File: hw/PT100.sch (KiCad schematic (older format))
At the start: 2 parts, among them U1501 ZXCT1086

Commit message: pcb first revision created, ready to order
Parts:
- removed U1501: ZXCT1086, usevolt:SOT-25, symbol ZXCT1086
- added U1601: ZXCT1086, usevolt:SOT-25, symbol ZXCT1086
- renumbered R1501 to R1401
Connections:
- net +3V3: now also U1601.5 (VCC)
- net GND: now also U1601.2 (GND), U1601.4 (S-)
- net VOUT: now also U1601.1 (OUT)
- net SENSE+ renamed SENSOR
- net SENSOR: now also U1601.3 (S+)
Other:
- moved on the sheet: R1701
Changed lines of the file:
@@
 EESchema Schematic File Version 2
-LIBS:msb-rescue
 LIBS:kemet
 LIBS:multicomp
@@
 LIBS:power
 LIBS:elt21300_kicad
-LIBS:msb-cache
+LIBS:esb-cache
 EELAYER 26 0
 EELAYER END
 $Descr A4 11693 8268
 encoding utf-8
-Sheet 15 16
+Sheet 16 17
 Title ""
 Date ""
@@
 Comment4 ""
 $EndDescr
-Text HLabel 6300 3250 0    60   Input ~ 0
-SENSE+
-Text HLabel 6300 4100 0    60   Input ~ 0
-SENSE-
-Text HLabel 7650 3700 2    60   Output ~ 0
+Text HLabel 7800 3600 2    60   Input ~ 0
+SENSOR
+Text HLabel 6450 3700 0    60   Output ~ 0
 VOUT
+Wire Wire Line
+	7450 3600 7800 3600
+Wire Wire Line
+	7600 3600 7600 3250
 $Comp
-L 10K R1501
-U 1 1 58C98806
-P 6500 3050
-AR Path="/58C97F3A/58C98806" Ref="R1501"  Part="1"
-AR Path="/58CA60CA/58C98806" Ref="R1601"  Part="1"
-F 0 "R1601" V 6508 3108 45  0000 L CNN
-F 1 "10K" V 6592 3108 45  0000 L CNN
-F 2 "multicomp:0603" H 6530 3200 20  0001 C CNN
-F 3 "http://www.farnell.com/datasheets/1788326.pdf?_ga=1.214208087.1948984246.1460023966" H 6469 3089 60  0001 C CNN
-F 4 "9330399" H 6869 3489 60  0001 C CNN "1st Source Part Number"
-F 5 "Farnell" H 6769 3389 60  0001 C CNN "1st Source"
-F 6 "MC0063W0603110K" H 6669 3289 60  0001 C CNN "Manufacturer Part Number"
-F 7 "MULTICOMP" H 6569 3189 60  0001 C CNN "Manufacturer"
-	1    6500 3050
-	0    1    1    0
+L GND #PWR1402
+U 1 1 58C99E8C
+P 6750 4000
+AR Path="/58C97F3A/58C99E8C" Ref="#PWR1402"  Part="1"
+AR Path="/58CA60CA/58C99E8C" Ref="#PWR1502"  Part="1"
+AR Path="/594BBBEF/58C99E8C" Ref="#PWR1602"  Part="1"
+AR Path="/594D630A/58C99E8C" Ref="#PWR1702"  Part="1"
+F 0 "#PWR1702" H 6750 3750 50  0001 C CNN
+F 1 "GND" H 6755 3827 50  0000 C CNN
+F 2 "" H 6750 4000 50  0000 C CNN
+F 3 "" H 6750 4000 50  0000 C CNN
+	1    6750 4000
+	-1   0    0    -1
+$EndComp
+Wire Wire Line
+	6750 4000 6750 3800
+Wire Wire Line
+	6750 3800 6900 3800
+$Comp
+L +3V3 #PWR1401
+U 1 1 58C99EAF
+P 6750 3400
+AR Path="/58C97F3A/58C99EAF" Ref="#PWR1401"  Part="1"
+AR Path="/58CA60CA/58C99EAF" Ref="#PWR1501"  Part="1"
+AR Path="/594BBBEF/58C99EAF" Ref="#PWR1601"  Part="1"
+AR Path="/594D630A/58C99EAF" Ref="#PWR1701"  Part="1"
+F 0 "#PWR1701" H 6750 3250 50  0001 C CNN
+F 1 "+3V3" H 6765 3573 50  0000 C CNN
+F 2 "" H 6750 3400 50  0000 C CNN
+F 3 "" H 6750 3400 50  0000 C CNN
+	1    6750 3400
+	-1   0    0    -1
+$EndComp
+Wire Wire Line
+	6750 3400 6750 3600
+Wire Wire Line
+	6750 3600 6900 3600
+Wire Wire Line
+	6450 3700 6900 3700
+Wire Wire Line
+	7600 2850 7600 2950
+$Comp
+L +3V3 #PWR1403
+U 1 1 58C98CB1
+P 7600 2850
+AR Path="/58C97F3A/58C98CB1" Ref="#PWR1403"  Part="1"
+AR Path="/58CA60CA/58C98CB1" Ref="#PWR1503"  Part="1"
+AR Path="/594BBBEF/58C98CB1" Ref="#PWR1603"  Part="1"
+AR Path="/594D630A/58C98CB1" Ref="#PWR1703"  Part="1"
+F 0 "#PWR1703" H 7600 2700 50  0001 C CNN
+F 1 "+3V3" H 7615 3023 50  0000 C CNN
+F 2 "" H 7600 2850 50  0000 C CNN
+F 3 "" H 7600 2850 50  0000 C CNN
+	1    7600 2850
+	-1   0    0    -1
 $EndComp
 $Comp
-L +3V3 #PWR1501
-U 1 1 58C98CB1
-P 6500 2850
-AR Path="/58C97F3A/58C98CB1" Ref="#PWR1501"  Part="1"
-AR Path="/58CA60CA/58C98CB1" Ref="#PWR1601"  Part="1"
-F 0 "#PWR1601" H 6500 2700 50  0001 C CNN
-F 1 "+3V3" H 6515 3023 50  0000 C CNN
-F 2 "" H 6500 2850 50  0000 C CNN
-F 3 "" H 6500 2850 50  0000 C CNN
-	1    6500 2850
+L 10K R1401
+U 1 1 58C98806
+P 7600 3050
+AR Path="/58C97F3A/58C98806" Ref="R1401"  Part="1"
+AR Path="/58CA60CA/58C98806" Ref="R1501"  Part="1"
+AR Path="/594BBBEF/58C98806" Ref="R1601"  Part="1"
+AR Path="/594D630A/58C98806" Ref="R1701"  Part="1"
+F 0 "R1701" V 7608 3108 45  0000 L CNN
+F 1 "10K" V 7692 3108 45  0000 L CNN
+F 2 "multicomp:0603" H 7630 3200 20  0001 C CNN
+F 3 "http://www.farnell.com/datasheets/1788326.pdf?_ga=1.214208087.1948984246.1460023966" H 7569 3089 60  0001 C CNN
+F 4 "9330399" H 7969 3489 60  0001 C CNN "1st Source Part Number"
+F 5 "Farnell" H 7869 3389 60  0001 C CNN "1st Source"
+F 6 "MC0063W0603110K" H 7769 3289 60  0001 C CNN "Manufacturer Part Number"
+F 7 "MULTICOMP" H 7669 3189 60  0001 C CNN "Manufacturer"
+	1    7600 3050
+	0    -1   1    0
+$EndComp
+Connection ~ 7600 3600
+$Comp
+L GND #PWR1404
+U 1 1 5944CE5C
+P 7600 3900
+AR Path="/58C97F3A/5944CE5C" Ref="#PWR1404"  Part="1"
+AR Path="/58CA60CA/5944CE5C" Ref="#PWR1504"  Part="1"
+AR Path="/594BBBEF/5944CE5C" Ref="#PWR1604"  Part="1"
+AR Path="/594D630A/5944CE5C" Ref="#PWR1704"  Part="1"
+F 0 "#PWR1704" H 7600 3650 50  0001 C CNN
+F 1 "GND" H 7605 3727 50  0000 C CNN
+F 2 "" H 7600 3900 50  0000 C CNN
+F 3 "" H 7600 3900 50  0000 C CNN
+	1    7600 3900
 	1    0    0    -1
 $EndComp
 Wire Wire Line
-	6500 2850 6500 2950
+	7600 3900 7600 3800
 Wire Wire Line
-	6500 3250 6300 3250
+	7600 3800 7450 3800
 $Comp
-L ZXCT1086 U1501
-U 1 1 58C999D0
-P 6900 3650
-AR Path="/58C97F3A/58C999D0" Ref="U1501"  Part="1"
-AR Path="/58CA60CA/58C999D0" Ref="U1601"  Part="1"
-F 0 "U1601" H 6875 3937 60  0000 C CNN
-F 1 "ZXCT1086" H 6875 3831 60  0000 C CNN
-F 2 "usevolt:SOT-25" H 6550 4100 60  0001 C CNN
-F 3 "http://www.farnell.com/datasheets/1383709.pdf?_ga=1.188141032.1948984246.1460023966" H 7300 3975 60  0001 C CNN
-F 4 "1904029" H 7300 4200 60  0001 C CNN "1st Source Part Number"
-F 5 "Digikey" H 7400 4300 60  0001 C CNN "2nd Source"
-F 6 "DIODES INC" H 7000 3900 60  0001 C CNN "Manufacturer"
-F 7 "Farnell" H 7200 4100 60  0001 C CNN "1st Source"
-F 8 "ZXCT1086E5TA" H 7100 4000 60  0001 C CNN "Manufacturer Part Number"
-F 9 "ZXCT1086E5TACT-ND" H 7500 4400 60  0001 C CNN "2nd Source Part Number"
-	1    6900 3650
-	-1   0    0    -1
-$EndComp
-Wire Wire Line
-	6650 3600 6500 3600
-Wire Wire Line
-	6500 3600 6500 3250
-Wire Wire Line
-	6650 3800 6500 3800
-Wire Wire Line
-	6500 3800 6500 4100
-Wire Wire Line
-	6500 4100 6300 4100
-$Comp
-L GND #PWR1503
-U 1 1 58C99E8C
-P 7350 4000
-AR Path="/58C97F3A/58C99E8C" Ref="#PWR1503"  Part="1"
-AR Path="/58CA60CA/58C99E8C" Ref="#PWR1603"  Part="1"
-F 0 "#PWR1603" H 7350 3750 50  0001 C CNN
-F 1 "GND" H 7355 3827 50  0000 C CNN
-F 2 "" H 7350 4000 50  0000 C CNN
-F 3 "" H 7350 4000 50  0000 C CNN
-	1    7350 4000
+L ZXCT1086 U1601
+U 1 1 5953DA3A
+P 7200 3650
+AR Path="/594BBBEF/5953DA3A" Ref="U1601"  Part="1"
+AR Path="/58C97F3A/5953DA3A" Ref="U1401"  Part="1"
+AR Path="/58CA60CA/5953DA3A" Ref="U1501"  Part="1"
+AR Path="/594D630A/5953DA3A" Ref="U1701"  Part="1"
+F 0 "U1701" H 7175 3937 60  0000 C CNN
+F 1 "ZXCT1086" H 7175 3831 60  0000 C CNN
+F 2 "usevolt:SOT-25" H 6850 4100 60  0001 C CNN
+F 3 "http://www.farnell.com/datasheets/1383709.pdf?_ga=1.188141032.1948984246.1460023966" H 7600 3975 60  0001 C CNN
+F 4 "1904029" H 7600 4200 60  0001 C CNN "1st Source Part Number"
+F 5 "Digikey" H 7700 4300 60  0001 C CNN "2nd Source"
+F 6 "DIODES INC" H 7300 3900 60  0001 C CNN "Manufacturer"
+F 7 "Farnell" H 7500 4100 60  0001 C CNN "1st Source"
+F 8 "ZXCT1086E5TA" H 7400 4000 60  0001 C CNN "Manufacturer Part Number"
+F 9 "ZXCT1086E5TACT-ND" H 7800 4400 60  0001 C CNN "2nd Source Part Number"
+	1    7200 3650
 	1    0    0    -1
 $EndComp
-Wire Wire Line
-	7350 4000 7350 3800
-Wire Wire Line
-	7350 3800 7200 3800
-$Comp
-L +3V3 #PWR1502
-U 1 1 58C99EAF
-P 7350 3400
-AR Path="/58C97F3A/58C99EAF" Ref="#PWR1502"  Part="1"
-AR Path="/58CA60CA/58C99EAF" Ref="#PWR1602"  Part="1"
-F 0 "#PWR1602" H 7350 3250 50  0001 C CNN
-F 1 "+3V3" H 7365 3573 50  0000 C CNN
-F 2 "" H 7350 3400 50  0000 C CNN
-F 3 "" H 7350 3400 50  0000 C CNN
-	1    7350 3400
-	1    0    0    -1
-$EndComp
-Wire Wire Line
-	7350 3400 7350 3600
-Wire Wire Line
-	7350 3600 7200 3600
-Wire Wire Line
-	7650 3700 7200 3700
 $EndSCHEMATC

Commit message: hw modifications from first version
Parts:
- removed U1601: ZXCT1086, usevolt:SOT-25, symbol ZXCT1086
- added U1401: ZXCT1086, usevolt:SOT-25, symbol ZXCT1086
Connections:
- net +3V3: now also U1401.5 (VCC)
- net GND: now also U1401.2 (GND), U1401.4 (S-)
- net SENSOR: now also U1401.3 (S+)
- net VOUT: now also U1401.1 (OUT)
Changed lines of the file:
@@
 $Descr A4 11693 8268
 encoding utf-8
-Sheet 16 17
+Sheet 14 17
 Title ""
 Date ""
@@
 	7600 3800 7450 3800
 $Comp
-L ZXCT1086 U1601
-U 1 1 5953DA3A
+L ZXCT1086 U1401
+U 1 1 597B0B49
 P 7200 3650
-AR Path="/594BBBEF/5953DA3A" Ref="U1601"  Part="1"
-AR Path="/58C97F3A/5953DA3A" Ref="U1401"  Part="1"
-AR Path="/58CA60CA/5953DA3A" Ref="U1501"  Part="1"
-AR Path="/594D630A/5953DA3A" Ref="U1701"  Part="1"
+AR Path="/58C97F3A/597B0B49" Ref="U1401"  Part="1"
+AR Path="/58CA60CA/597B0B49" Ref="U1501"  Part="1"
+AR Path="/594BBBEF/597B0B49" Ref="U1601"  Part="1"
+AR Path="/594D630A/597B0B49" Ref="U1701"  Part="1"
 F 0 "U1701" H 7175 3937 60  0000 C CNN
 F 1 "ZXCT1086" H 7175 3831 60  0000 C CNN

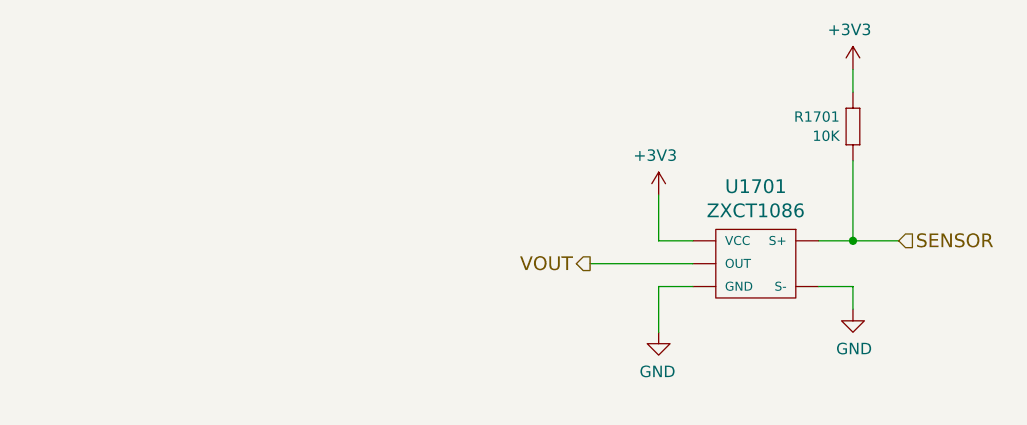
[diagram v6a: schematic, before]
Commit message: 4.0.0 ordered from itead
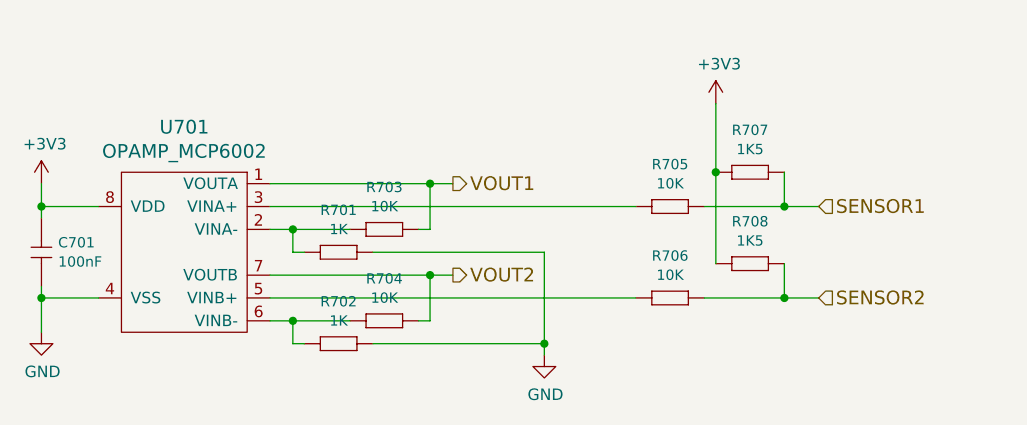
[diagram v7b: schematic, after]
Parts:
- removed R1401: 10K, multicomp:0603, symbol 10K
- removed U1401: ZXCT1086, usevolt:SOT-25, symbol ZXCT1086
- added C701: 100nF, kemet:0603, symbol 100nF
- added R701, R702: 1K, yageo:0603, symbol 1K
- added R703, R704, R705, R706: 10K, yageo:0603, symbol 10K
- added R707, R708: 1K5, yageo:0603, symbol 1K5
- added U701: OPAMP_MCP6002, usevolt:SOIC8, symbol OPAMP_MCP6002
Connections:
- net +3V3: now also C701.2 (C2), R707.2 (R2), R708.2 (R2), U701.8 (VDD)
- net GND: now also C701.1 (C1), R701.1 (R1), R702.1 (R1), U701.4 (VSS)
- new net: R701.2 (R2), R703.2 (R2), U701.2 (VINA-)
- new net: R705.2 (R2), U701.3 (VINA+)
- new net: R706.2 (R2), U701.5 (VINB+)
- new net: R702.2 (R2), R704.2 (R2), U701.6 (VINB-)
- new net SENSOR1: R705.1 (R1), R707.1 (R1)
- new net SENSOR2: R706.1 (R1), R708.1 (R1)
- new net VOUT1: R703.1 (R1), U701.1 (VOUTA)
- new net VOUT2: R704.1 (R1), U701.7 (VOUTB)
